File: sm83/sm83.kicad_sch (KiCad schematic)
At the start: 0 parts

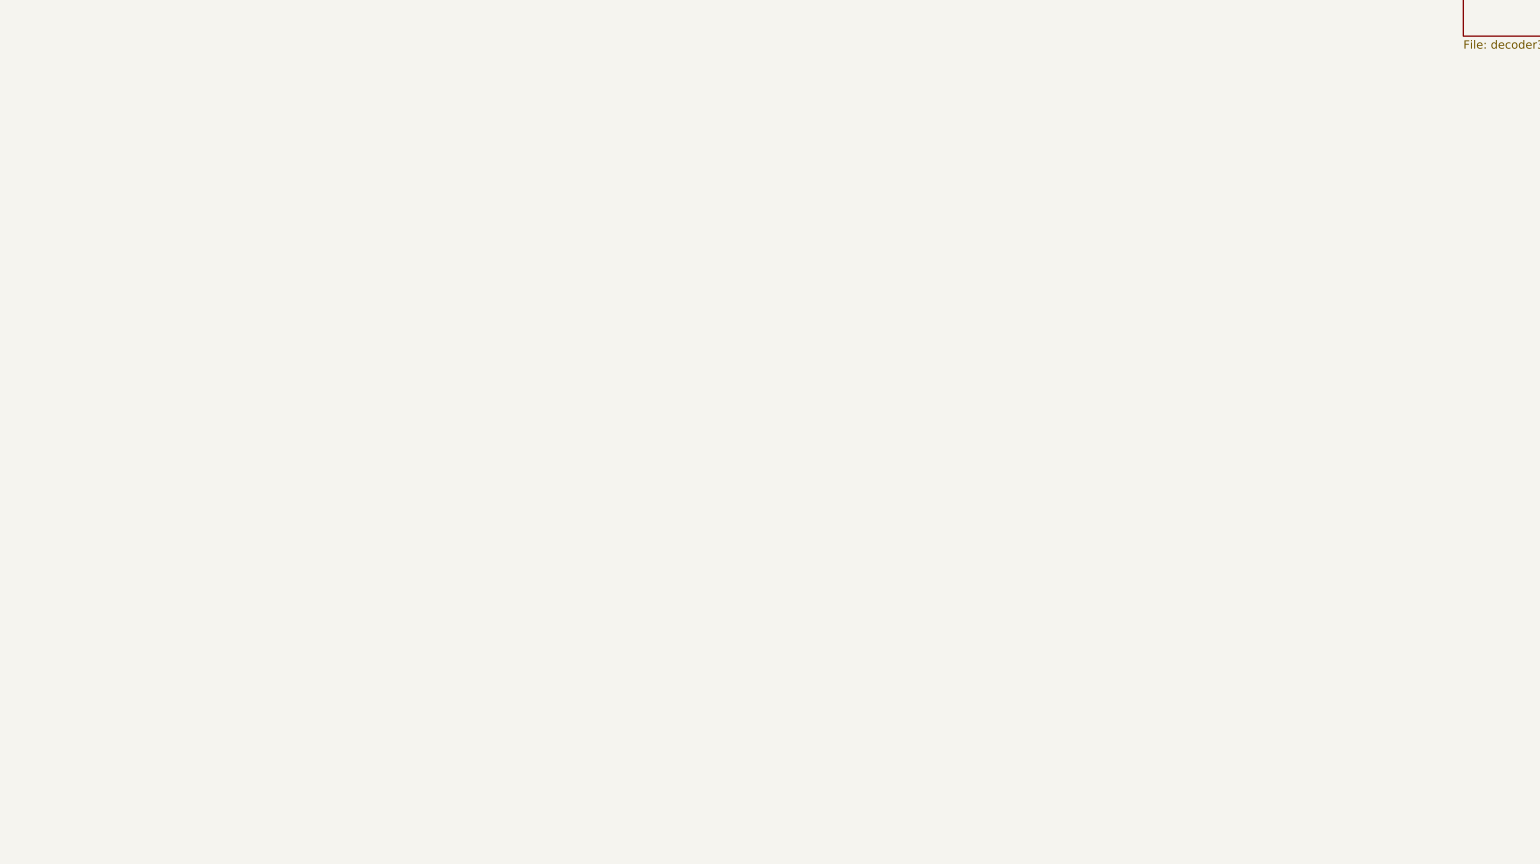
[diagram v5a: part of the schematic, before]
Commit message: SM83: Add schematic of general purpose registers
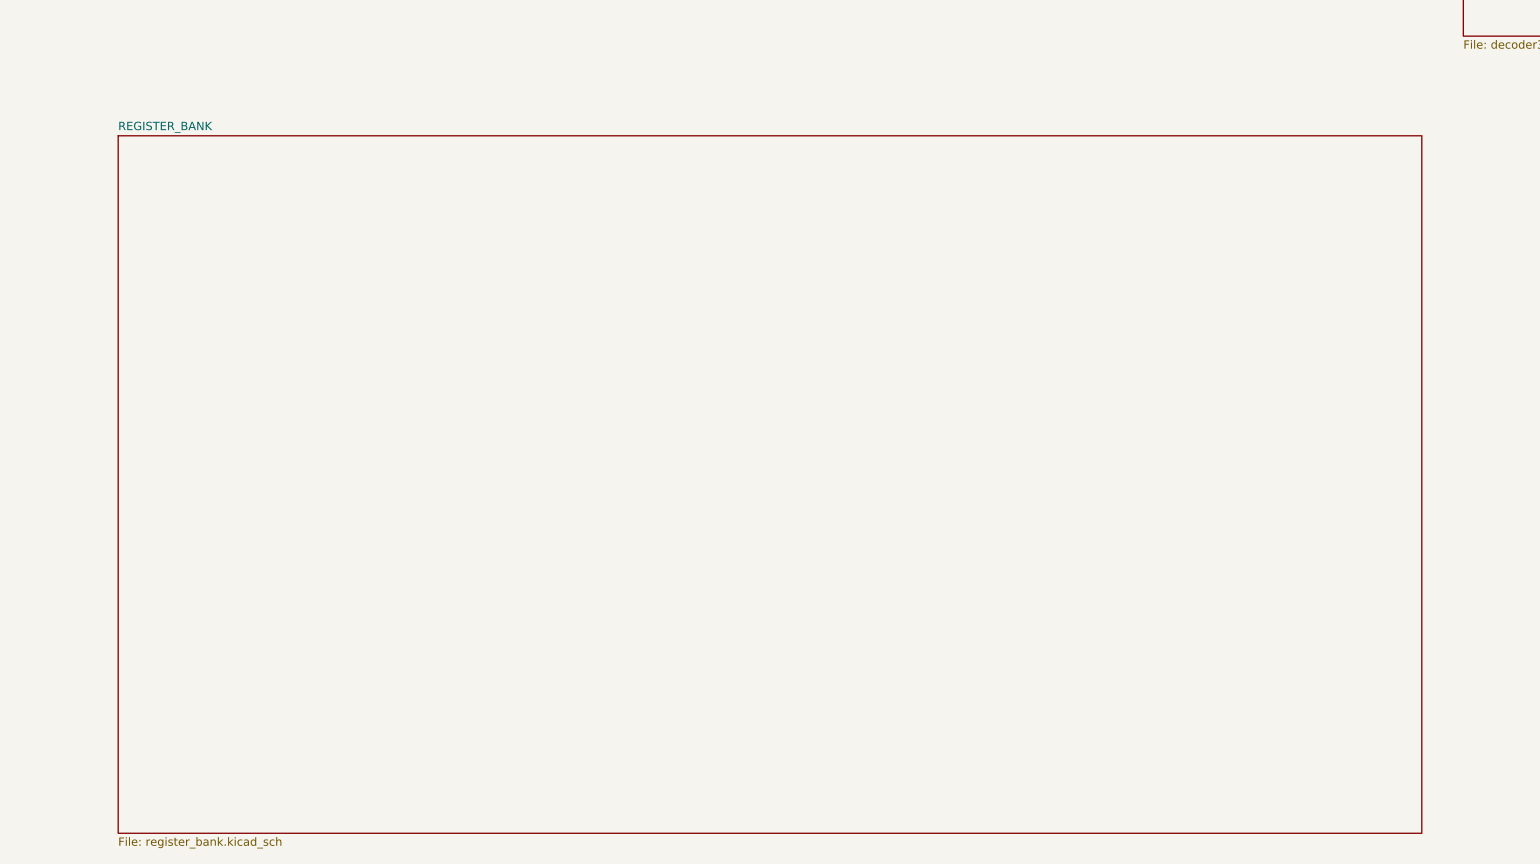
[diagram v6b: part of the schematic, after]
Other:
- added sheet REGISTER_BANK (register_bank.kicad_sch)
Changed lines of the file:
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@@
+	)
+	(sheet
+		(at 93.98 452.12)
+		(size 199.39 106.68)
+		(exclude_from_sim no)
+		(in_bom yes)
+		(on_board yes)
+		(dnp no)
+		(fields_autoplaced yes)
+		(stroke
+			(width 0.1524)
+			(type solid)
+		)
+		(fill
+			(color 0 0 0 0.0000)
+		)
+		(property "Sheetname" "REGISTER_BANK"
+			(at 93.98 451.4084 0)
+			(effects
+				(font
+					(size 1.27 1.27)
+				)
+				(justify left bottom)
+			)
+		)
+		(property "Sheetfile" "register_bank.kicad_sch"
+			(at 93.98 559.3846 0)
+			(effects
+				(font
+					(size 1.27 1.27)
+				)
+				(justify left top)
+			)
+		)
+		(instances
+			(project "sm83"
+				(path "/8717d046-1dfd-46fe-a5f7-4e4d2f07de68"
+					(page "9")
+				)
+			)
+		)
 	)
 	(sheet

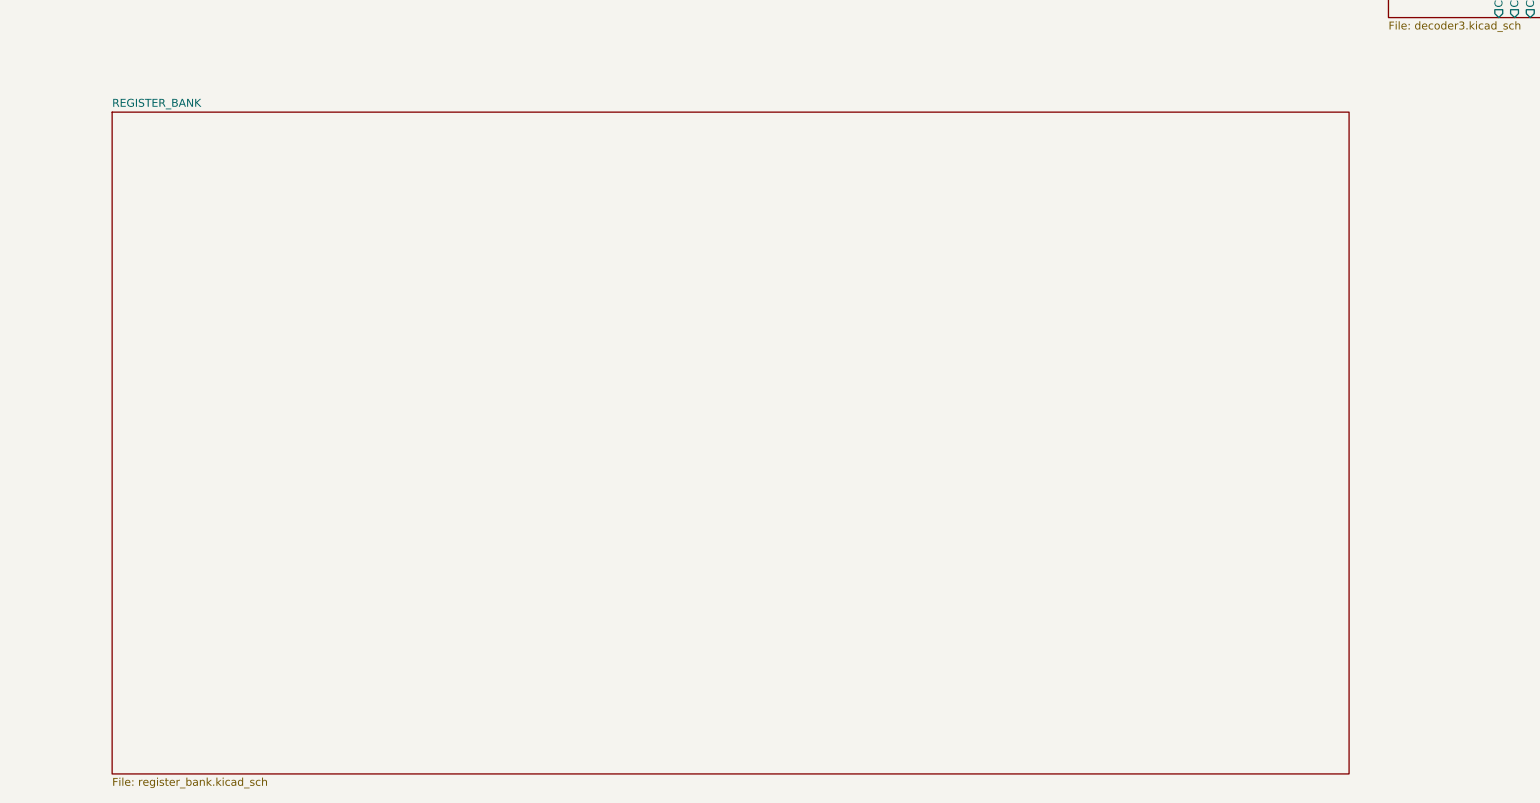
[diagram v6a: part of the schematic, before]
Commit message: SM83: Finish schematics of register bank
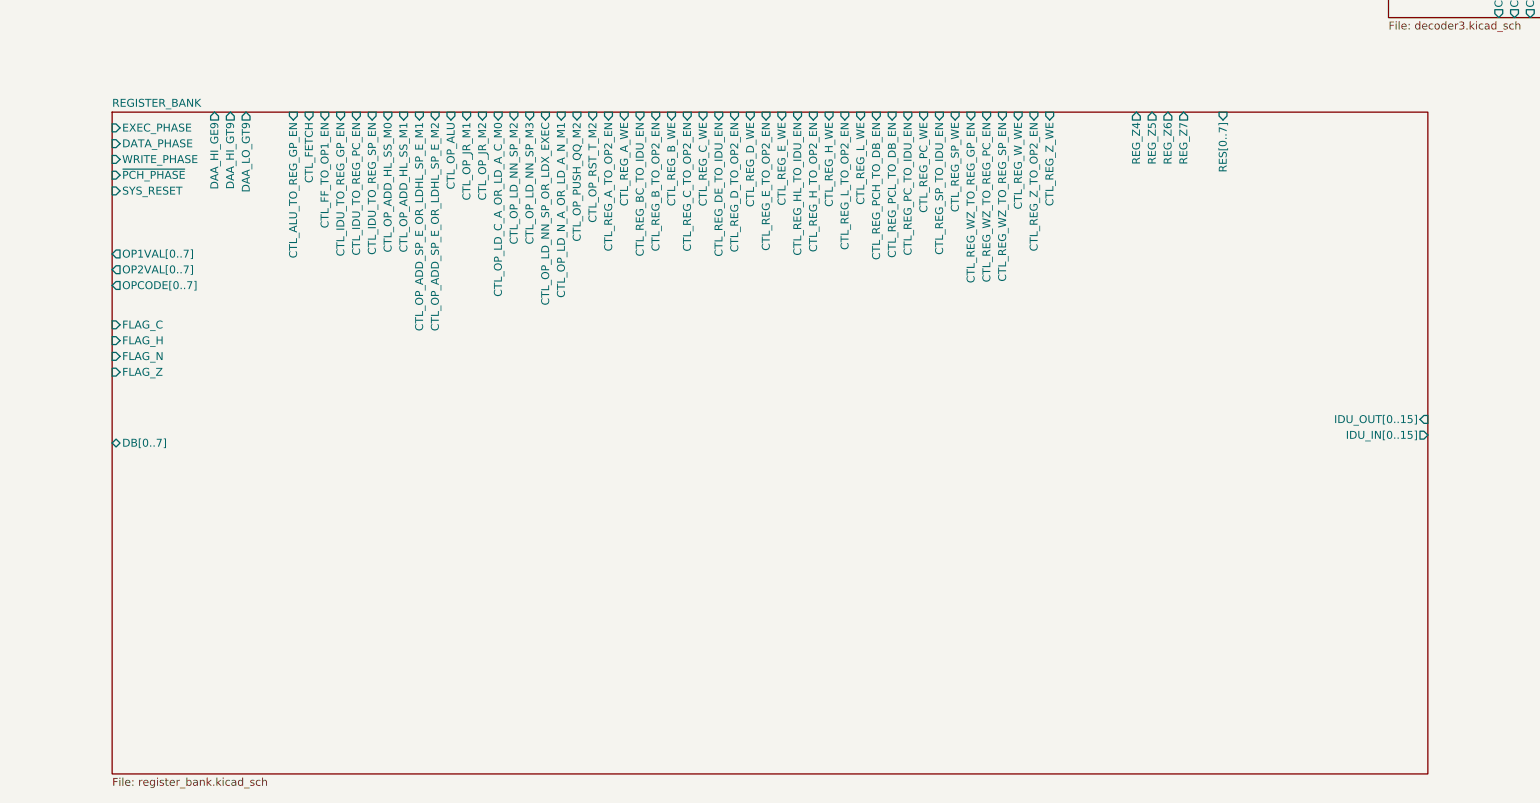
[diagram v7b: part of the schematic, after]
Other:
- sheet REGISTER_BANK ports: added CTL_ALU_TO_REG_GP_EN, CTL_FETCH, CTL_FF_TO_OP1_EN, CTL_IDU_TO_REG_GP_EN, CTL_IDU_TO_REG_PC_EN, CTL_IDU_TO_REG_SP_EN, CTL_OP_ADD_HL_SS_M0, CTL_OP_ADD_HL_SS_M1, CTL_OP_ADD_SP_E_OR_LDHL_SP_E_M1, CTL_OP_ADD_SP_E_OR_LDHL_SP_E_M2, CTL_OP_ALU, CTL_OP_JR_M1, CTL_OP_JR_M2, CTL_OP_LD_C_A_OR_LD_A_C_M0, CTL_OP_LD_NN_SP_M2, CTL_OP_LD_NN_SP_M3, CTL_OP_LD_NN_SP_OR_LDX_EXEC, CTL_OP_LD_N_A_OR_LD_A_N_M1, CTL_OP_PUSH_QQ_M2, CTL_OP_RST_T_M2, CTL_REG_A_TO_OP2_EN, CTL_REG_A_WE, CTL_REG_BC_TO_IDU_EN, CTL_REG_B_TO_OP2_EN, CTL_REG_B_WE, CTL_REG_C_TO_OP2_EN, CTL_REG_C_WE, CTL_REG_DE_TO_IDU_EN, CTL_REG_D_TO_OP2_EN, CTL_REG_D_WE, CTL_REG_E_TO_OP2_EN, CTL_REG_E_WE, CTL_REG_HL_TO_IDU_EN, CTL_REG_H_TO_OP2_EN, CTL_REG_H_WE, CTL_REG_L_TO_OP2_EN, CTL_REG_L_WE, CTL_REG_PCH_TO_DB_EN, CTL_REG_PCL_TO_DB_EN, CTL_REG_PC_TO_IDU_EN, CTL_REG_PC_WE, CTL_REG_SP_TO_IDU_EN, CTL_REG_SP_WE, CTL_REG_WZ_TO_REG_GP_EN, CTL_REG_WZ_TO_REG_PC_EN, CTL_REG_WZ_TO_REG_SP_EN, CTL_REG_W_WE, CTL_REG_Z_TO_OP2_EN, CTL_REG_Z_WE, DAA_HI_GE9, DAA_HI_GT9, DAA_LO_GT9, DATA_PHASE, DB[0..7], EXEC_PHASE, FLAG_C, FLAG_H, FLAG_N, FLAG_Z, IDU_IN[0..15], IDU_OUT[0..15], OP1VAL[0..7], OP2VAL[0..7], OPCODE[0..7], REG_Z4, REG_Z5, REG_Z6, REG_Z7, RES[0..7], SYS_RESET, WRITE_PHASE, ~{PCH_PHASE}; removed none

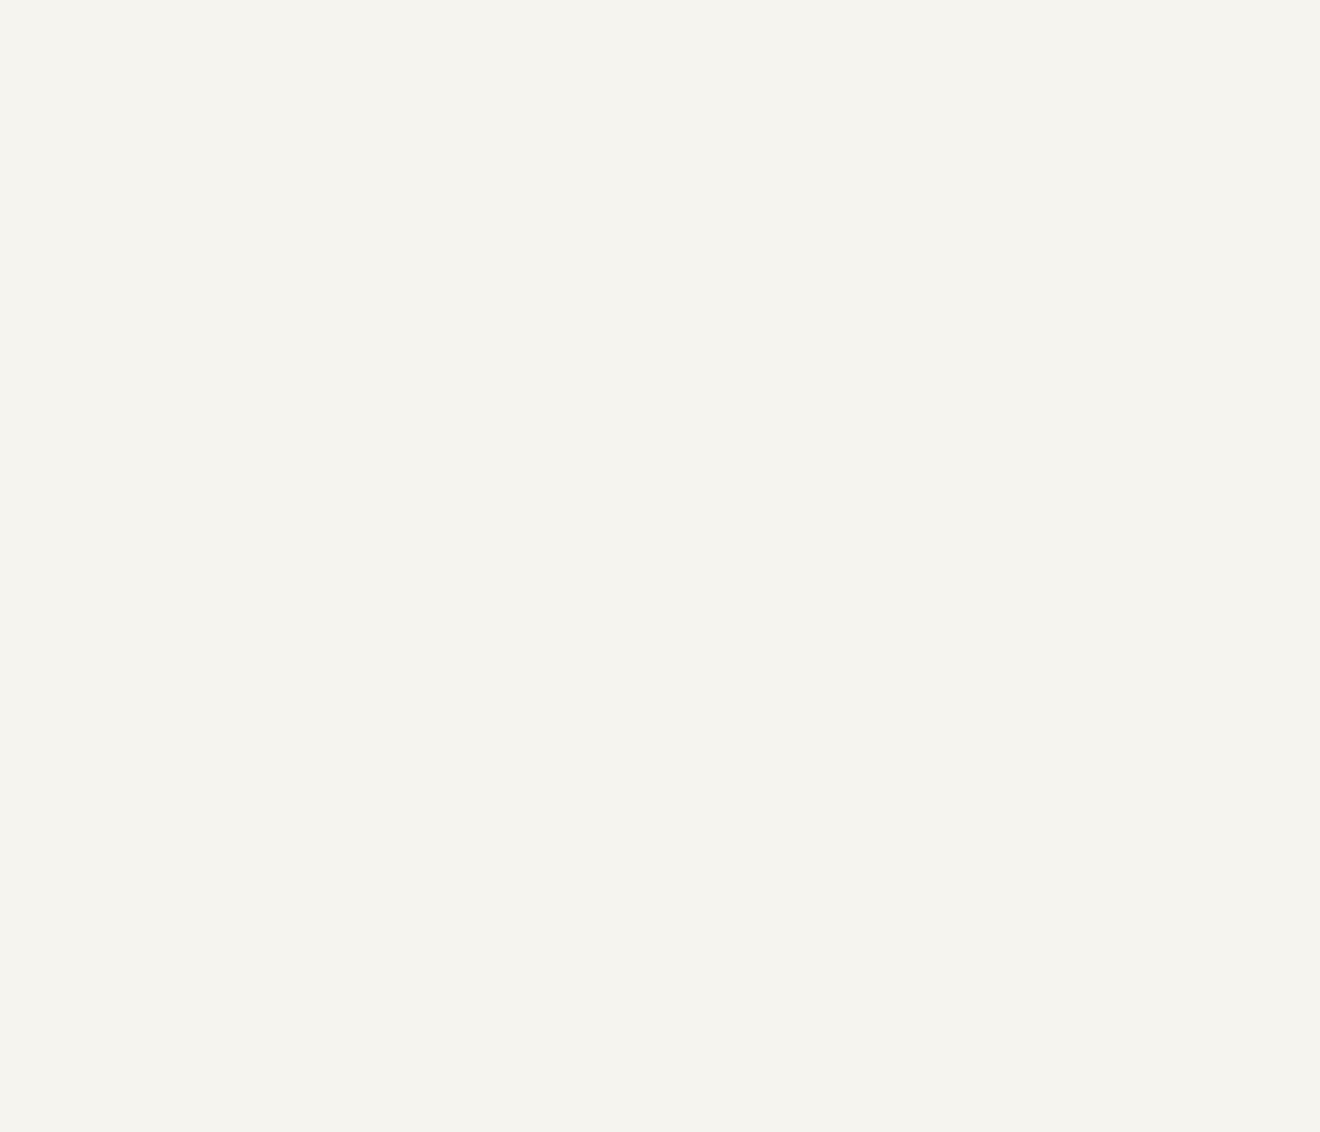
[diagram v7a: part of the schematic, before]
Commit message: SM83: Add schematic of IDU
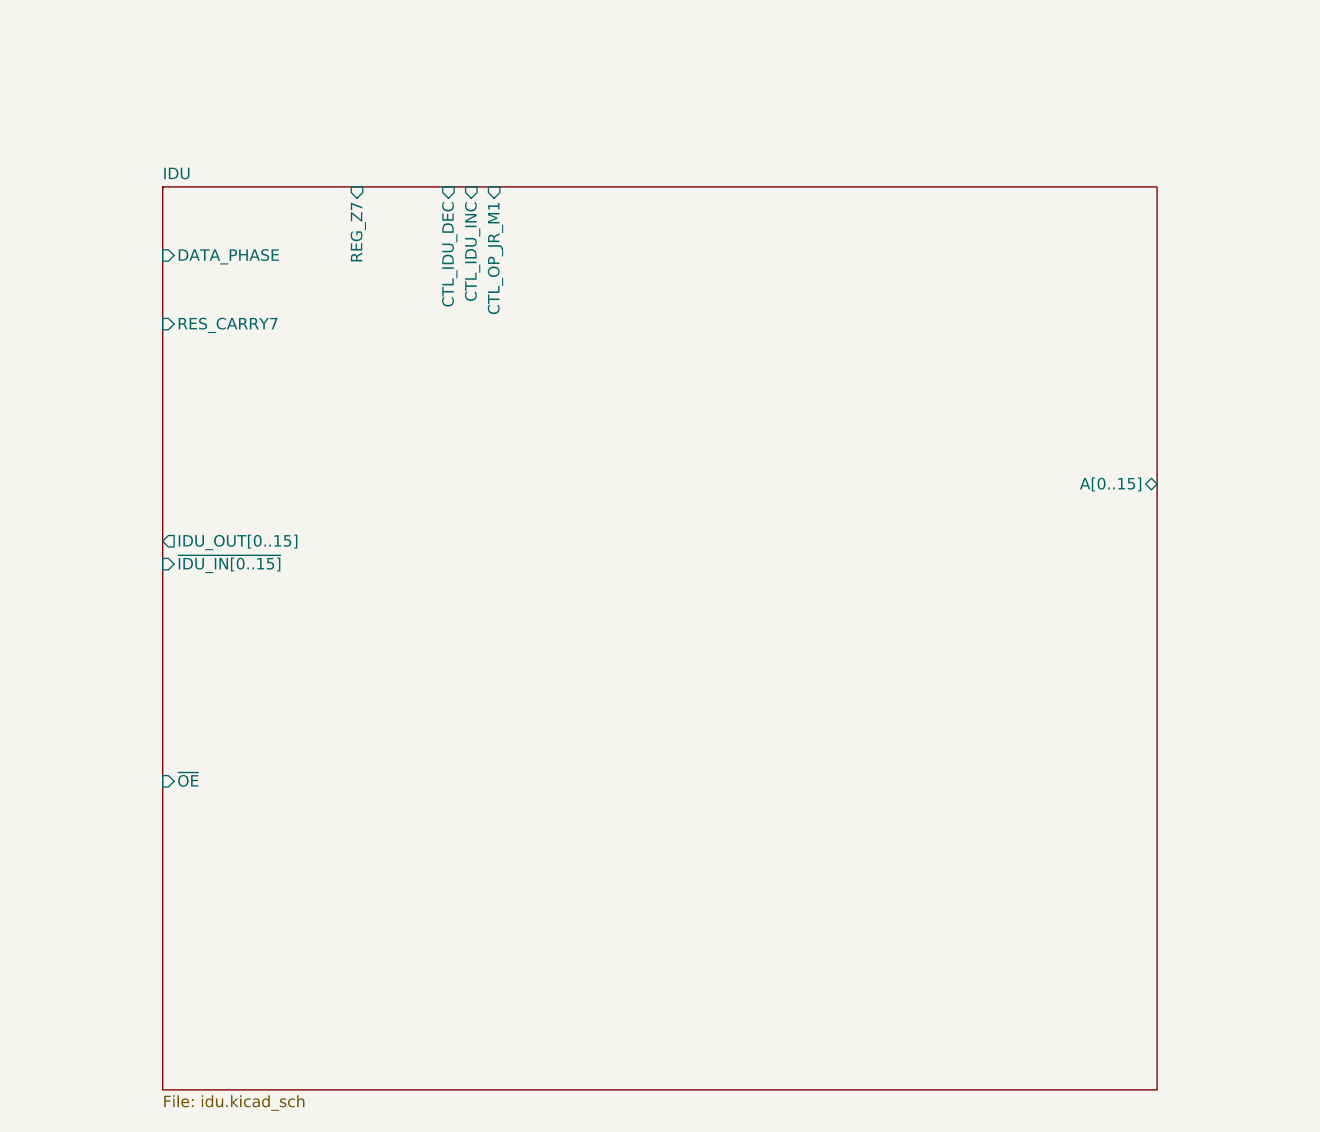
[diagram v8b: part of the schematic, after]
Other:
- added sheet IDU (idu.kicad_sch)
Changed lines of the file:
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@@
+	)
+	(sheet
+		(at 372.11 462.28)
+		(size 110.49 100.33)
+		(exclude_from_sim no)
+		(in_bom yes)
+		(on_board yes)
+		(dnp no)
+		(fields_autoplaced yes)
+		(stroke
+			(width 0.1524)
+			(type solid)
+		)
+		(fill
+			(color 0 0 0 0.0000)
+		)
+		(property "Sheetname" "IDU"
+			(at 372.11 461.5684 0)
+			(effects
+				(font
+					(size 1.27 1.27)
+				)
+				(justify left bottom)
+			)
+		)
+		(property "Sheetfile" "idu.kicad_sch"
+			(at 372.11 563.1946 0)
+			(effects
+				(font
+					(size 1.27 1.27)
+				)
+				(justify left top)
+			)
+		)
+		(pin "A[0..15]" tri_state
+			(at 482.6 495.3 0)
+			(effects
+				(font
+					(size 1.27 1.27)
+				)
+				(justify right)
+			)
+		)
+		(pin "CTL_IDU_DEC" input
+			(at 403.86 462.28 90)
+			(effects
+				(font
+					(size 1.27 1.27)
+				)
+				(justify right)
+			)
+		)
+		(pin "CTL_IDU_INC" input
+			(at 406.4 462.28 90)
+			(effects
+				(font
+					(size 1.27 1.27)
+				)
+				(justify right)
+			)
+		)
+		(pin "CTL_OP_JR_M1" input
+			(at 408.94 462.28 90)
+			(effects
+				(font
+					(size 1.27 1.27)
+				)
+				(justify right)
+			)
+		)
+		(pin "DATA_PHASE" input
+			(at 372.11 469.9 180)
+			(effects
+				(font
+					(size 1.27 1.27)
+				)
+				(justify left)
+			)
+		)
+		(pin "IDU_OUT[0..15]" output
+			(at 372.11 501.65 180)
+			(effects
+				(font
+					(size 1.27 1.27)
+				)
+				(justify left)
+			)
+		)
+		(pin "REG_Z7" input
+			(at 393.7 462.28 90)
+			(effects
+				(font
+					(size 1.27 1.27)
+				)
+				(justify right)
+			)
+		)
+		(pin "RES_CARRY7" input
+			(at 372.11 477.52 180)
+			(effects
+				(font
+					(size 1.27 1.27)
+				)
+				(justify left)
+			)
+		)
+		(pin "~{IDU_IN[0..15]}" input
+			(at 372.11 504.19 180)
+			(effects
+				(font
+					(size 1.27 1.27)
+				)
+				(justify left)
+			)
+		)
+		(pin "~{OE}" input
+			(at 372.11 528.32 180)
+			(effects
+				(font
+					(size 1.27 1.27)
+				)
+				(justify left)
+			)
+		)
+		(instances
+			(project "sm83"
+				(path "/8717d046-1dfd-46fe-a5f7-4e4d2f07de68"
+					(page "13")
+				)
+			)
+		)
 	)
 	(sheet
